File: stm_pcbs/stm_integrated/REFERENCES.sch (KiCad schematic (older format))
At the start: 17 parts, among them U13 AD8676, U14 AD8675

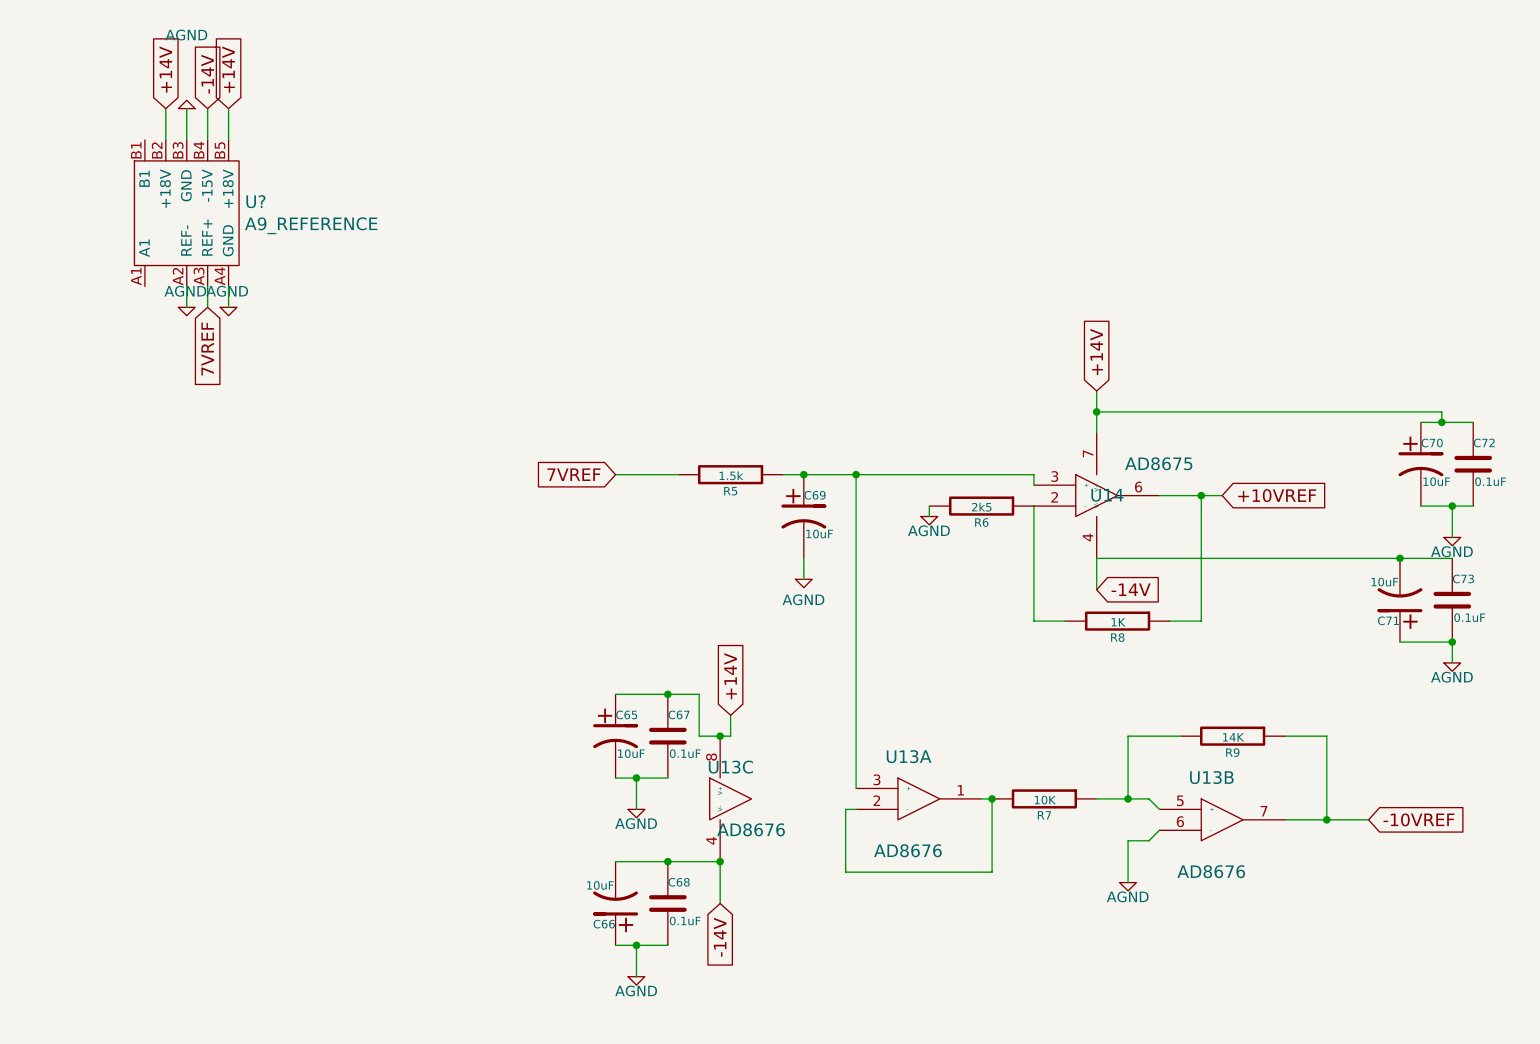
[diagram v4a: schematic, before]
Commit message: fixed issue with DAC (opamp wiring was wrong)
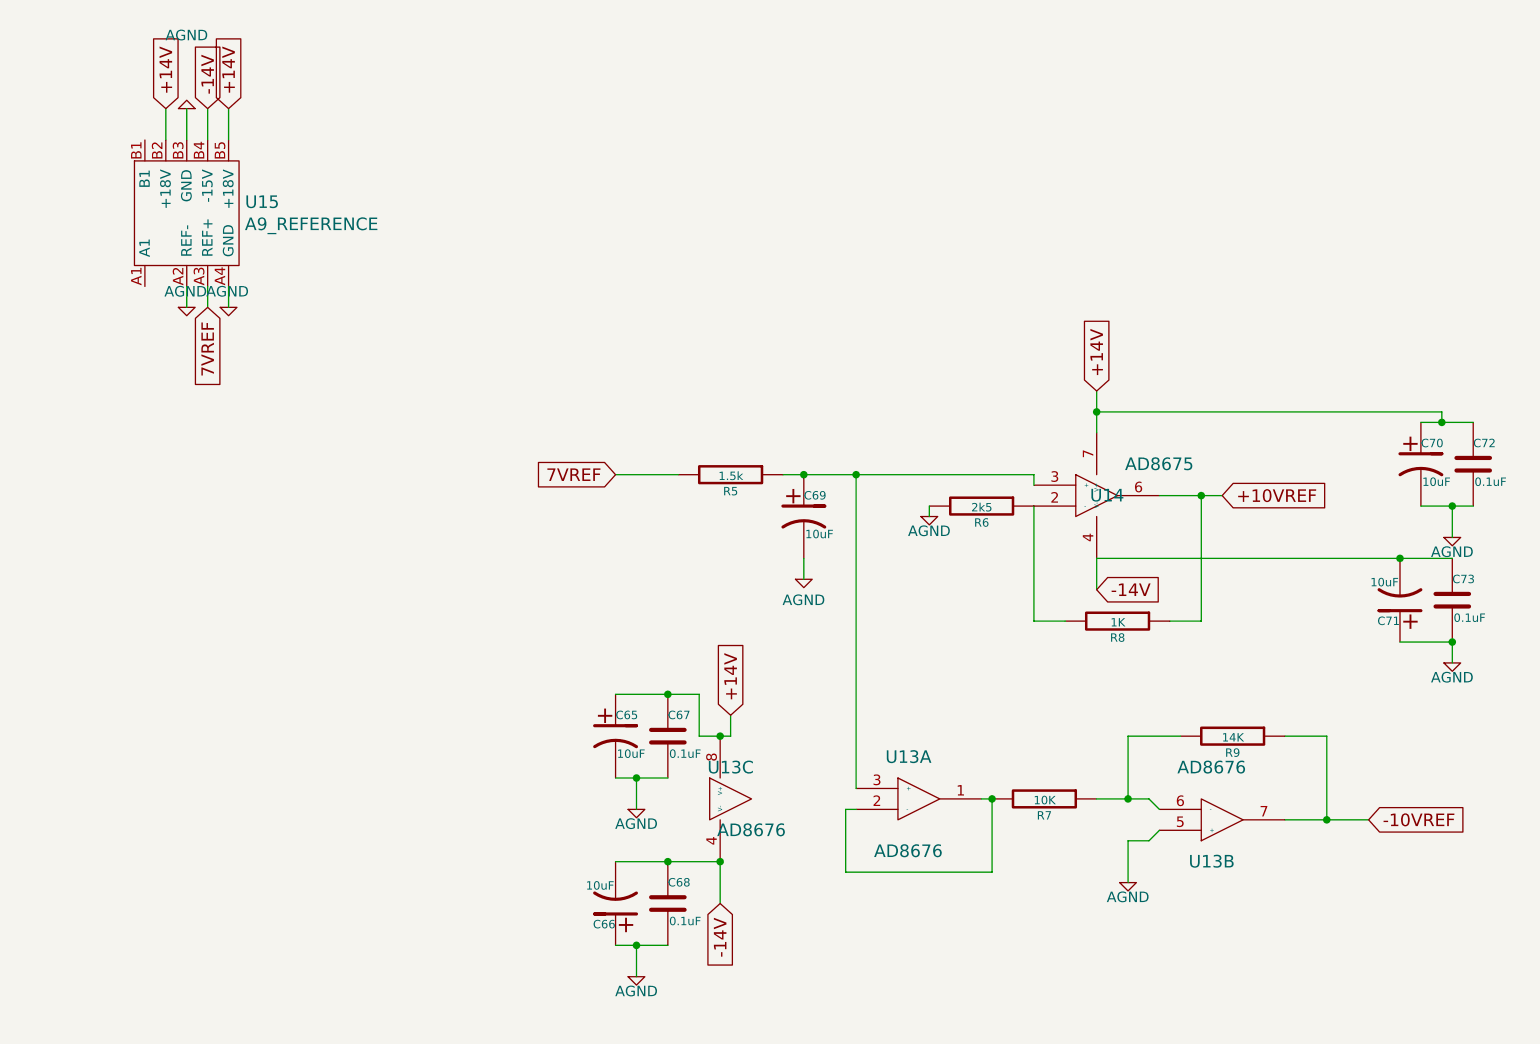
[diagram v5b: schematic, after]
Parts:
- U15: renamed from U?; footprint (none) -> A9_REFERENCE:A9REFERENCE
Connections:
- net AGND: now also U13.5 (+); no longer U13.6 (-)
- net at R7.1, R9.2: now also U13.6 (-); no longer U13.5 (+)
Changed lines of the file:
@@
 F 3 "" H 6700 4600 60  0000 C CNN
 	2    6550 4600
-	1    0    0    -1
+	1    0    0    1
 $EndComp
 $Comp
@@
 +14V
 $Comp
-L LTC1859:AGND #PWR?
+L LTC1859:AGND #PWR056
 U 1 1 5A2C3626
 P 1650 1200
-F 0 "#PWR?" H 1650 1200 40  0001 C CNN
+F 0 "#PWR056" H 1650 1200 40  0001 C CNN
 F 1 "AGND" H 1650 850 50  0000 C CNN
 F 2 "" H 1650 1200 60  0000 C CNN
@@
 +14V
 $Comp
-L LTC1859:AGND #PWR?
+L LTC1859:AGND #PWR057
 U 1 1 5A2CA845
 P 1850 2150
-F 0 "#PWR?" H 1850 2150 40  0001 C CNN
+F 0 "#PWR057" H 1850 2150 40  0001 C CNN
 F 1 "AGND" H 1845 2225 50  0000 C CNN
 F 2 "" H 1850 2150 60  0000 C CNN
@@
 7VREF
 $Comp
-L LTC1859:AGND #PWR?
+L LTC1859:AGND #PWR058
 U 1 1 5A2CCBC6
 P 1650 2150
-F 0 "#PWR?" H 1650 2150 40  0001 C CNN
+F 0 "#PWR058" H 1650 2150 40  0001 C CNN
 F 1 "AGND" H 1645 2225 50  0000 C CNN
 F 2 "" H 1650 2150 60  0000 C CNN
@@
 $EndComp
 $Comp
-L A9_REFERENCE:A9_REFERENCE U?
+L A9_REFERENCE:A9_REFERENCE U15
 U 1 1 5A2A6FA3
 P 1650 1700
-F 0 "U?" H 1928 1753 60  0000 L CNN
+F 0 "U15" H 1928 1753 60  0000 L CNN
 F 1 "A9_REFERENCE" H 1928 1647 60  0000 L CNN
-F 2 "" H 1650 1700 60  0001 C CNN
+F 2 "A9_REFERENCE:A9REFERENCE" H 1650 1700 60  0001 C CNN
 F 3 "" H 1650 1700 60  0001 C CNN
 	1    1650 1700

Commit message: Mostly Chua's stuff
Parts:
- C65, C66, C69, C70, C71: symbol device:CP1 -> Device:CP
- C67, C68, C72, C73: symbol device:C -> Device:C
- R5, R6, R7, R8, R9: symbol device:R -> Device:R
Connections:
- net AGND: no longer C65.2, C66.1, C67.2, C68.2, C69.2, C70.2, C71.1, C72.2, C73.2, R6.2, U13.5 (+)
- new net GNDA: C65.2, C66.1, C67.2, C68.2, C69.2, C70.2, C71.1, C72.2, C73.2, R6.2, U13.5 (+)
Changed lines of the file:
@@
 EESchema Schematic File Version 4
-LIBS:stmshieldfull-cache
-EELAYER 26 0
+EELAYER 30 0
 EELAYER END
 $Descr A4 11693 8268
@@
 $EndComp
 $Comp
-L device:R R5
+L Device:R R5
 U 1 1 5A25B558
 P 4250 2950
@@
 $EndComp
 $Comp
-L power:AGND #PWR049
+L power:GNDA #PWR049
 U 1 1 5A25B55F
 P 4600 3450
 F 0 "#PWR049" H 4600 3450 40  0001 C CNN
-F 1 "AGND" H 4600 3350 50  0000 C CNN
+F 1 "GNDA" H 4600 3350 50  0000 C CNN
 F 2 "" H 4600 3450 60  0000 C CNN
 F 3 "" H 4600 3450 60  0000 C CNN
@@
 $EndComp
 $Comp
-L device:R R6
+L Device:R R6
 U 1 1 5A25B565
 P 5450 3100
@@
 $EndComp
 $Comp
-L device:R R8
+L Device:R R8
 U 1 1 5A25B56C
 P 6100 3650
@@
 $EndComp
 $Comp
-L device:R R7
+L Device:R R7
 U 1 1 5A25B573
 P 5750 4500
@@
 $EndComp
 $Comp
-L power:AGND #PWR050
+L power:GNDA #PWR050
 U 1 1 5A25B57A
 P 5200 3150
 F 0 "#PWR050" H 5200 3150 40  0001 C CNN
-F 1 "AGND" H 5200 3080 50  0000 C CNN
+F 1 "GNDA" H 5200 3080 50  0000 C CNN
 F 2 "" H 5200 3150 60  0000 C CNN
 F 3 "" H 5200 3150 60  0000 C CNN
@@
 $EndComp
 $Comp
-L power:AGND #PWR051
+L power:GNDA #PWR051
 U 1 1 5A25B580
 P 6150 4900
 F 0 "#PWR051" H 6150 4900 40  0001 C CNN
-F 1 "AGND" H 6150 4830 50  0000 C CNN
+F 1 "GNDA" H 6150 4700 50  0000 C CNN
 F 2 "" H 6150 4900 60  0000 C CNN
 F 3 "" H 6150 4900 60  0000 C CNN
@@
 $EndComp
 $Comp
-L device:R R9
+L Device:R R9
 U 1 1 5A25B586
 P 6650 4200
@@
 -14V
 $Comp
-L device:C C67
+L Device:C C67
 U 1 1 5A25B594
 P 3950 4200
@@
 $EndComp
 $Comp
-L device:C C68
+L Device:C C68
 U 1 1 5A25B59B
 P 3950 5000
@@
 $EndComp
 $Comp
-L power:AGND #PWR052
+L power:GNDA #PWR052
 U 1 1 5A25B5A2
 P 3800 5350
 F 0 "#PWR052" H 3800 5350 40  0001 C CNN
-F 1 "AGND" H 3800 5280 50  0000 C CNN
+F 1 "GNDA" H 3800 5200 50  0000 C CNN
 F 2 "" H 3800 5350 60  0000 C CNN
 F 3 "" H 3800 5350 60  0000 C CNN
@@
 $EndComp
 $Comp
-L power:AGND #PWR053
+L power:GNDA #PWR053
 U 1 1 5A25B5A8
 P 3800 4550
 F 0 "#PWR053" H 3800 4550 40  0001 C CNN
-F 1 "AGND" H 3800 4480 50  0000 C CNN
+F 1 "GNDA" H 3800 4400 50  0000 C CNN
 F 2 "" H 3800 4550 60  0000 C CNN
 F 3 "" H 3800 4550 60  0000 C CNN
@@
 $EndComp
 $Comp
-L device:CP1 C66
+L Device:CP C66
 U 1 1 5A25B5AE
 P 3700 5000
@@
 $EndComp
 $Comp
-L device:CP1 C65
+L Device:CP C65
 U 1 1 5A25B5B5
 P 3700 4200
@@
 $EndComp
 $Comp
-L device:C C72
+L Device:C C72
 U 1 1 5A25B5BC
 P 7800 2900
@@
 $EndComp
 $Comp
-L device:C C73
+L Device:C C73
 U 1 1 5A25B5C3
 P 7700 3550
@@
 $EndComp
 $Comp
-L power:AGND #PWR054
+L power:GNDA #PWR054
 U 1 1 5A25B5CA
-P 7700 3250
-F 0 "#PWR054" H 7700 3250 40  0001 C CNN
-F 1 "AGND" H 7700 3180 50  0000 C CNN
-F 2 "" H 7700 3250 60  0000 C CNN
-F 3 "" H 7700 3250 60  0000 C CNN
-	1    7700 3250
-	1    0    0    -1
-$EndComp
-$Comp
-L power:AGND #PWR055
+P 7700 3200
+F 0 "#PWR054" H 7700 3200 40  0001 C CNN
+F 1 "GNDA" H 7800 3200 50  0000 C CNN
+F 2 "" H 7700 3200 60  0000 C CNN
+F 3 "" H 7700 3200 60  0000 C CNN
+	1    7700 3200
+	1    0    0    -1
+$EndComp
+$Comp
+L power:GNDA #PWR055
 U 1 1 5A25B5D0
 P 7700 3850
 F 0 "#PWR055" H 7700 3850 40  0001 C CNN
-F 1 "AGND" H 7700 3780 50  0000 C CNN
+F 1 "GNDA" H 7700 3700 50  0000 C CNN
 F 2 "" H 7700 3850 60  0000 C CNN
 F 3 "" H 7700 3850 60  0000 C CNN
@@
 $EndComp
 $Comp
-L device:CP1 C70
+L Device:CP C70
 U 1 1 5A25B5D6
 P 7550 2900
@@
 $EndComp
 $Comp
-L device:CP1 C71
+L Device:CP C71
 U 1 1 5A25B5DD
 P 7450 3550
@@
 Wire Wire Line
 	6150 4200 6150 4500
-Wire Wire Line
-	6150 4200 6400 4200
 Connection ~ 6500 3050
 Wire Wire Line
@@
 Wire Wire Line
 	3700 5200 3800 5200
-Wire Wire Line
-	3700 4800 3950 4800
-Connection ~ 3950 4800
 Wire Wire Line
 	3800 5350 3800 5200
@@
 Connection ~ 3800 4400
 Wire Wire Line
-	3700 4000 3950 4000
-Wire Wire Line
 	4100 4000 4100 4200
 Wire Wire Line
 	4100 4200 4200 4200
-Connection ~ 3950 4000
 Wire Wire Line
 	5700 2950 5700 3000
-Connection ~ 5500 4500
 Wire Wire Line
 	6250 4500 6300 4550
@@
 	4850 4550 4800 4550
 Wire Wire Line
-	4600 3450 4600 3350
-Wire Wire Line
 	4850 2950 5700 2950
 Wire Wire Line
 	6500 3050 6600 3050
 Wire Wire Line
-	3950 4800 4200 4800
-Wire Wire Line
 	3800 5200 3950 5200
 Wire Wire Line
 	3800 4400 3950 4400
 Wire Wire Line
-	3950 4000 4100 4000
-Wire Wire Line
 	6150 4500 6250 4500
 Wire Wire Line
@@
 Wire Wire Line
 	6000 2650 6000 2750
-Wire Wire Line
-	7700 3100 7700 3250
-$Comp
-L device:CP1 C69
+$Comp
+L Device:CP C69
 U 1 1 5A25B62B
 P 4600 3150
@@
 	1    0    0    -1
 $EndComp
-Wire Wire Line
-	4850 2950 4600 2950
 Connection ~ 4850 2950
 Wire Wire Line
-	4600 2950 4500 2950
-Connection ~ 4600 2950
-Wire Wire Line
-	4000 2950 3700 2950
-Wire Wire Line
 	5700 3650 5700 3100
 Wire Wire Line
 	5200 3150 5200 3100
 Wire Wire Line
-	6500 3650 6350 3650
-Wire Wire Line
-	5850 3650 5700 3650
-Wire Wire Line
 	6000 3350 6000 3500
-Connection ~ 7700 3750
-Wire Wire Line
-	7700 3350 7450 3350
-Connection ~ 7450 3350
-Wire Wire Line
-	6000 3350 7450 3350
-Wire Wire Line
-	7800 3100 7700 3100
-Wire Wire Line
-	7700 3100 7550 3100
-Connection ~ 7700 3100
 Wire Wire Line
 	7550 2700 7650 2700
@@
 Wire Wire Line
 	7650 2700 7800 2700
-Wire Wire Line
-	6900 4200 7100 4200
-Wire Wire Line
-	6000 4500 6150 4500
 Text GLabel 1850 1200 1    60   Input ~ 0
 +14V
@@
 Wire Wire Line
 	1750 2150 1750 2050
+Wire Wire Line
+	3700 4800 3950 4800
+Wire Wire Line
+	3700 4000 3950 4000
+Wire Wire Line
+	6000 3350 7450 3350
+Wire Wire Line
+	5700 3100 5600 3100
+Connection ~ 5700 3100
+Wire Wire Line
+	5300 3100 5200 3100
+Wire Wire Line
+	3700 2950 4100 2950
+Wire Wire Line
+	4600 3000 4600 2950
+Connection ~ 4600 2950
+Wire Wire Line
+	4600 2950 4850 2950
+Wire Wire Line
+	4400 2950 4600 2950
+Wire Wire Line
+	4600 3300 4600 3450
+Wire Wire Line
+	6250 3650 6500 3650
+Wire Wire Line
+	5700 3650 5950 3650
+Wire Wire Line
+	7800 2750 7800 2700
+Wire Wire Line
+	7550 2700 7550 2750
+Wire Wire Line
+	7550 3050 7550 3100
+Wire Wire Line
+	7800 3050 7800 3100
+Wire Wire Line
+	7700 3350 7700 3400
+Wire Wire Line
+	7450 3350 7450 3400
+Connection ~ 7450 3350
+Wire Wire Line
+	7450 3350 7700 3350
+Wire Wire Line
+	7450 3700 7450 3750
+Wire Wire Line
+	7700 3700 7700 3750
+Connection ~ 7700 3750
+Wire Wire Line
+	6800 4200 7100 4200
+Wire Wire Line
+	6150 4200 6500 4200
+Wire Wire Line
+	5900 4500 6150 4500
+Wire Wire Line
+	5600 4500 5500 4500
+Connection ~ 5500 4500
+Wire Wire Line
+	3700 4400 3700 4350
+Wire Wire Line
+	3700 4050 3700 4000
+Wire Wire Line
+	3950 5150 3950 5200
+Wire Wire Line
+	3950 4800 3950 4850
+Connection ~ 3950 4800
+Wire Wire Line
+	3950 4800 4200 4800
+Wire Wire Line
+	3700 4800 3700 4850
+Wire Wire Line
+	3700 5200 3700 5150
+Wire Wire Line
+	3950 4350 3950 4400
+Wire Wire Line
+	3950 4050 3950 4000
+Connection ~ 3950 4000
+Wire Wire Line
+	3950 4000 4100 4000
+Wire Wire Line
+	7550 3100 7700 3100
+Wire Wire Line
+	7700 3200 7700 3100
+Connection ~ 7700 3100
+Wire Wire Line
+	7700 3100 7800 3100
 $EndSCHEMATC
